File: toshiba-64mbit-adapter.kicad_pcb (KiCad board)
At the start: 2 copper layers, 18 x 55 mm, 9 parts, among them U1 TC5364205, U2 W29GL064C, U3 74HCT244, U4 74HCT244, U5 74HCT244, U6 74HCT244, U7 74HCT244, U8 TPS73633DBV

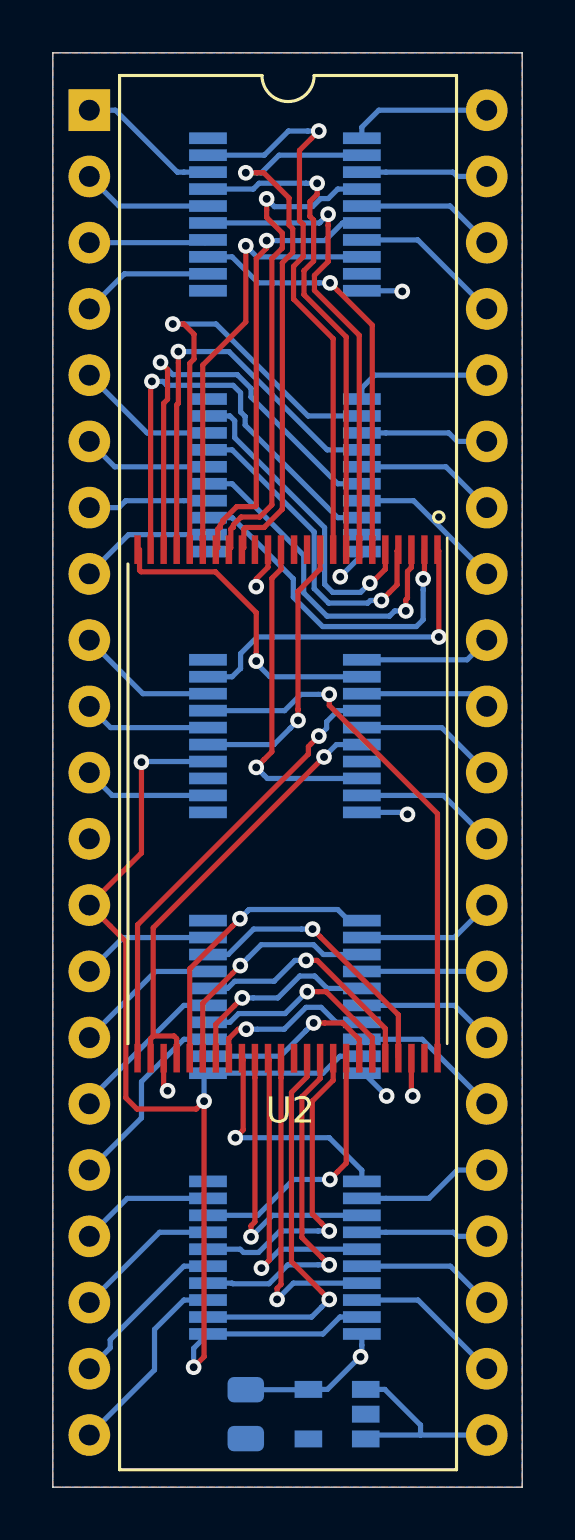
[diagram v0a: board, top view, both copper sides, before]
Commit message: Add 3 jumpers to allow picking between byte/word access
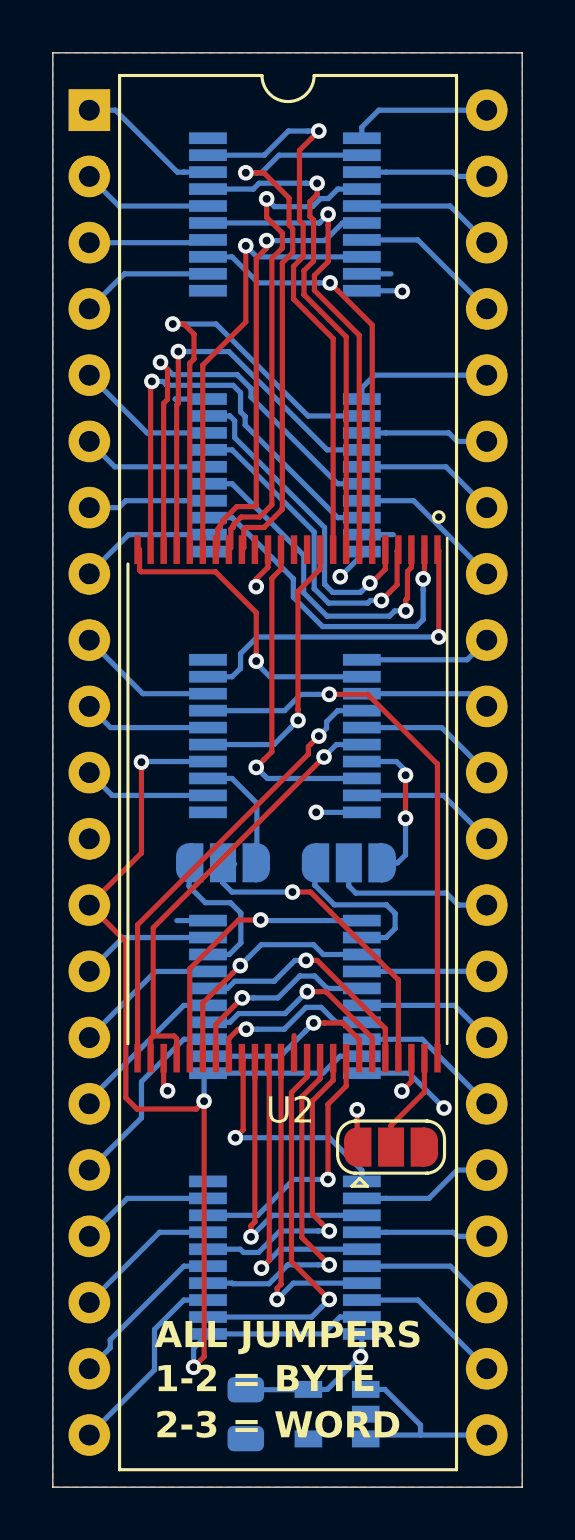
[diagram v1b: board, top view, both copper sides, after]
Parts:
- added JP1: SolderJumper_3_Open, Jumper:SolderJumper-3_P1.3mm_Open_RoundedPad1.0x1.5mm, B.Cu at (116.1, 89.9)
- added JP2: SolderJumper_3_Open, Jumper:SolderJumper-3_P1.3mm_Open_RoundedPad1.0x1.5mm, B.Cu at (121.0, 89.9)
- added JP3: SolderJumper_3_Open, Jumper:SolderJumper-3_P1.3mm_Open_RoundedPad1.0x1.5mm, F.Cu at (122.6, 100.8)
- U3, U4, U5, U6, U7: value 74HCT244 -> 74LVC244
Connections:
- U1 pad 30: /D15 -> /DA15
- U2 pad 15: Net-(U2-Pad15) -> unconnected-(U2-/BY-Pad15)
- U2 pad 45: /md15 -> /mad15
- U2 pad 47: +3V3 -> /BYTE
- U5 pad 17: GND -> /A-1
- U5 pad 3: Net-(U5-Pad3) -> /ma-1
- U8 pad 4: Net-(U8-Pad4) -> unconnected-(U8-NR-Pad4)
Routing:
- net /mad15: track 0.00 -> 12.2 mm, vias 0 -> 1
- net /DA15: track 0.00 -> 6.95 mm
- net GND: track 9.87 -> 16.0 mm, vias 3 -> 4
- net /A-1: track 0.00 -> 6.05 mm, vias 0 -> 2
- net /md15: track 10.7 -> 5.90 mm, vias 1 -> 0
- net /ma-1: track 0.00 -> 4.55 mm
- net /BYTE: track 0.00 -> 3.94 mm
- net +3V3: track 11.9 -> 15.1 mm
- net /D15: track 5.31 -> 6.38 mm
- net /ma16: track 20.6 -> 21.4 mm
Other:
- net class Default removed
- board text added: "1-2 = BYTE"
- board text added: "2-3 = WORD"
- board text added: "ALL JUMPERS"
- board text added: "CC0 v1.1 2019 ack v1"
- board text removed: "CC0 v1.1 2019"

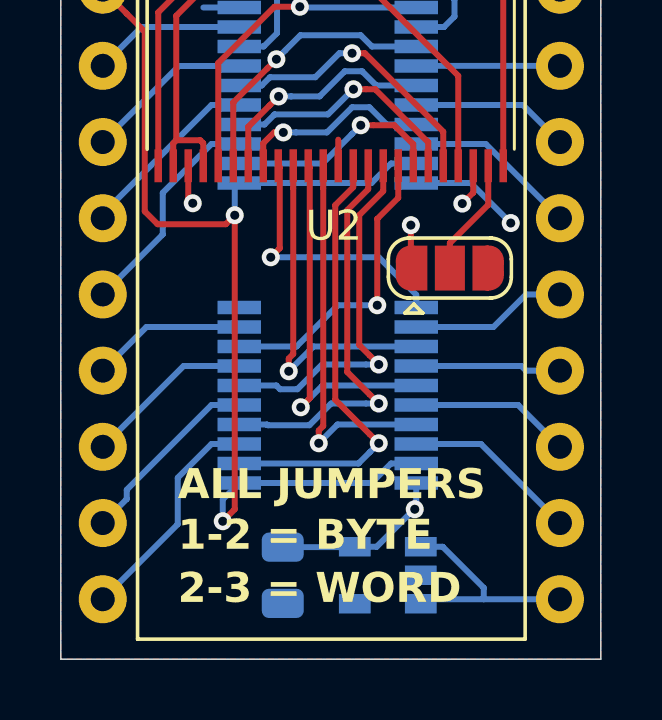
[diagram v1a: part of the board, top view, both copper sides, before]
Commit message: Switch the 2x data line LVC244s to HCT244s
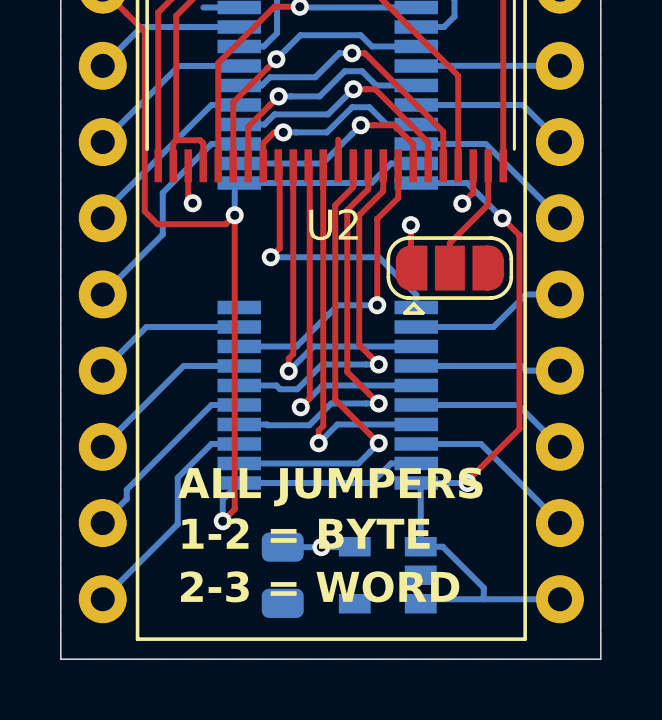
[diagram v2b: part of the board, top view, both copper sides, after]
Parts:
- U6, U7: value 74LVC244 -> 74HCT244
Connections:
- U6 pad 20: +3V3 -> +5V
- U7 pad 20: +3V3 -> +5V
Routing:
- net +5V: track 7.75 -> 24.6 mm, vias 0 -> 2
- net +3V3: track 15.1 -> 7.89 mm, vias 5 -> 4
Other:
- board text added: "CC0 v1.1 2019 ack v2"
- board text added: "HCT244"
- board text added: "LVC244"
- board text removed: "CC0 v1.1 2019 ack v1"
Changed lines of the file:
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@@
 		)
 		(sheetname "Root")
-		(sheetfile "/Users/jwestfall/Downloads/toshiba-64mbit-adapter-master/toshiba-64mbit-adapter.sch")
+		(sheetfile "toshiba-64mbit-adapter.kicad_sch")
 		(attr smd)
 		(fp_line
@@
 		)
 		(sheetname "Root")
-		(sheetfile "/Users/jwestfall/Downloads/toshiba-64mbit-adapter-master/toshiba-64mbit-adapter.sch")
+		(sheetfile "toshiba-64mbit-adapter.kicad_sch")
 		(attr through_hole)
 		(fp_line
@@
 		(property ki_fp_filters "SolderJumper*Open*")
 		(sheetname "Root")
-		(sheetfile "/Users/jwestfall/Downloads/toshiba-64mbit-adapter-master/toshiba-64mbit-adapter.sch")
+		(sheetfile "toshiba-64mbit-adapter.kicad_sch")
 		(zone_connect 1)
 		(attr exclude_from_pos_files exclude_from_bom)
@@
 		(property ki_fp_filters "TSSOP*4.4x6.5mm*P0.65mm* SSOP*4.4x6.5mm*P0.65mm*")
 		(sheetname "Root")
-		(sheetfile "/Users/jwestfall/Downloads/toshiba-64mbit-adapter-master/toshiba-64mbit-adapter.sch")
+		(sheetfile "toshiba-64mbit-adapter.kicad_sch")
 		(attr smd)
 		(fp_line
@@
 		(property ki_fp_filters "TSSOP*4.4x6.5mm*P0.65mm* SSOP*4.4x6.5mm*P0.65mm*")
 		(sheetname "Root")
-		(sheetfile "/Users/jwestfall/Downloads/toshiba-64mbit-adapter-master/toshiba-64mbit-adapter.sch")
+		(sheetfile "toshiba-64mbit-adapter.kicad_sch")
 		(attr smd)
 		(fp_line
@@
 			)
 		)
-		(property "Value" "74LVC244"
+		(property "Value" "74HCT244"
 			(at 0 -4.3 0)
 			(layer "B.Fab")
@@
 		(property ki_fp_filters "TSSOP*4.4x6.5mm*P0.65mm* SSOP*4.4x6.5mm*P0.65mm*")
 		(sheetname "Root")
-		(sheetfile "/Users/jwestfall/Downloads/toshiba-64mbit-adapter-master/toshiba-64mbit-adapter.sch")
+		(sheetfile "toshiba-64mbit-adapter.kicad_sch")
 		(attr smd)
 		(fp_line
@@
 			(size 1.45 0.45)
 			(layers "B.Cu" "B.Paste" "B.Mask")
-			(net 43 "+3V3")
+			(net 40 "+5V")
 			(pinfunction "VCC")
 			(pintype "power_in")
@@
 			)
 		)
-		(property "Value" "74LVC244"
+		(property "Value" "74HCT244"
 			(at 0 -4.3 0)
 			(layer "B.Fab")
@@
 		(property ki_fp_filters "TSSOP*4.4x6.5mm*P0.65mm* SSOP*4.4x6.5mm*P0.65mm*")
 		(sheetname "Root")
-		(sheetfile "/Users/jwestfall/Downloads/toshiba-64mbit-adapter-master/toshiba-64mbit-adapter.sch")
+		(sheetfile "toshiba-64mbit-adapter.kicad_sch")
 		(attr smd)
 		(fp_line
@@
 			(size 1.45 0.45)
 			(layers "B.Cu" "B.Paste" "B.Mask")
-			(net 43 "+3V3")
+			(net 40 "+5V")
 			(pinfunction "VCC")
 			(pintype "power_in")
@@
 		(property "Reference" "U8"
 			(at -2.7 0 -90)
+			(unlocked yes)
 			(layer "B.SilkS")
 			(effects
@@
 		(property ki_fp_filters "SOT?23*")
 		(sheetname "Root")
-		(sheetfile "/Users/jwestfall/Downloads/toshiba-64mbit-adapter-master/toshiba-64mbit-adapter.sch")
+		(sheetfile "toshiba-64mbit-adapter.kicad_sch")
 		(attr smd)
 		(fp_line
@@
 		(property ki_fp_filters "TSSOP*4.4x6.5mm*P0.65mm* SSOP*4.4x6.5mm*P0.65mm*")
 		(sheetname "Root")
-		(sheetfile "/Users/jwestfall/Downloads/toshiba-64mbit-adapter-master/toshiba-64mbit-adapter.sch")
+		(sheetfile "toshiba-64mbit-adapter.kicad_sch")
 		(attr smd)
 		(fp_line
@@
 		(tags "capacitor")
 		(property "Reference" "C1"
-			(at 0 -1.7 90)
+			(at 0 -1.7 -90)
+			(unlocked yes)
 			(layer "B.SilkS")
 			(effects
@@
 		(property ki_fp_filters "C_*")
 		(sheetname "Root")
-		(sheetfile "/Users/jwestfall/Downloads/toshiba-64mbit-adapter-master/toshiba-64mbit-adapter.sch")
+		(sheetfile "toshiba-64mbit-adapter.kicad_sch")
 		(attr smd)
 		(fp_line
@@
 		(property ki_fp_filters "SolderJumper*Open*")
 		(sheetname "Root")
-		(sheetfile "/Users/jwestfall/Downloads/toshiba-64mbit-adapter-master/toshiba-64mbit-adapter.sch")
+		(sheetfile "toshiba-64mbit-adapter.kicad_sch")
 		(zone_connect 1)
 		(attr exclude_from_pos_files exclude_from_bom)
@@
 		(property ki_fp_filters "SolderJumper*Open*")
 		(sheetname "Root")
-		(sheetfile "/Users/jwestfall/Downloads/toshiba-64mbit-adapter-master/toshiba-64mbit-adapter.sch")
+		(sheetfile "toshiba-64mbit-adapter.kicad_sch")
 		(zone_connect 1)
 		(attr exclude_from_pos_files exclude_from_bom)
@@
 		)
 	)
-	(gr_text "CC0 v1.1 2019 ack v1"
+	(gr_text "HCT244"
+		(at 117.9 108 270)
+		(layer "B.SilkS")
+		(effects
+			(font
+				(size 1 1)
+				(thickness 0.15)
+			)
+			(justify left bottom mirror)
+		)
+	)
+	(gr_text "CC0 v1.1 2019 ack v2"
 		(at 113.09 89.97 270)
 		(layer "B.SilkS")
@@
 		)
 	)
+	(gr_text "LVC244"
+		(at 117.9 77.9 270)
+		(layer "B.SilkS")
+		(effects
+			(font
+				(size 1 1)
+				(thickness 0.15)
+			)
+			(justify left bottom mirror)
+		)
+	)
+	(gr_text "LVC244"
+		(at 117.9 87.9 270)
+		(layer "B.SilkS")
+		(effects
+			(font
+				(size 1 1)
+				(thickness 0.15)
+			)
+			(justify left bottom mirror)
+		)
+	)
+	(gr_text "HCT244"
+		(at 117.9 98 270)
+		(layer "B.SilkS")
+		(effects
+			(font
+				(size 1 1)
+				(thickness 0.15)
+			)
+			(justify left bottom mirror)
+		)
+	)
+	(gr_text "LVC244"
+		(at 117.9 67.9 270)
+		(layer "B.SilkS")
+		(effects
+			(font
+				(size 1 1)
+				(thickness 0.15)
+			)
+			(justify left bottom mirror)
+		)
+	)
 	(gr_text "2-3 = WORD"
 		(at 113.5 112.01 0)
@@
 	)
 	(segment
+		(start 124.32103 99.09897)
+		(end 124.89 99.66794)
+		(width 0.2)
+		(layer "F.Cu")
+		(net 40)
+	)
+	(segment
+		(start 124.89 106.12)
+		(end 123.12 107.89)
+		(width 0.2)
+		(layer "F.Cu")
+		(net 40)
+	)
+	(segment
+		(start 124.89 99.66794)
+		(end 124.89 106.12)
+		(width 0.2)
+		(layer "F.Cu")
+		(net 40)
+	)
+	(via
+		(at 123.16 107.925)
+		(size 0.6)
+		(drill 0.3)
+		(layers "F.Cu" "B.Cu")
+		(net 40)
+	)
+	(via
+		(at 124.32103 99.09897)
+		(size 0.6)
+		(drill 0.3)
+		(layers "F.Cu" "B.Cu")
+		(net 40)
+	)
+	(segment
+		(start 124.32103 99.09897)
+		(end 124.321029 99.09897)
+		(width 0.2)
+		(layer "B.Cu")
+		(net 40)
+	)
+	(segment
+		(start 121.6 110.05)
+		(end 121.6 108.075)
+		(width 0.2)
+		(layer "B.Cu")
+		(net 40)
+	)
+	(segment
+		(start 121.45 107.925)
+		(end 123.16 107.925)
+		(width 0.2)
+		(layer "B.Cu")
+		(net 40)
+	)
+	(segment
+		(start 123.147059 97.925)
+		(end 121.45 97.925)
+		(width 0.2)
+		(layer "B.Cu")
+		(net 40)
+	)
+	(segment
+		(start 123.16 107.925)
+		(end 123.165 107.925)
+		(width 0.2)
+		(layer "B.Cu")
+		(net 40)
+	)
+	(segment
 		(start 126.24 111.8)
 		(end 123.7 111.8)
@@
 	)
 	(segment
+		(start 124.321029 99.09897)
+		(end 123.147059 97.925)
+		(width 0.2)
+		(layer "B.Cu")
+		(net 40)
+	)
+	(segment
 		(start 123.7 111.8)
 		(end 123.7 111.42)
@@
 	)
 	(via
-		(at 124.6 99.26)
+		(at 118.29 110.0625)
 		(size 0.6)
 		(drill 0.3)
@@
 	)
 	(via
-		(at 121.4 108.8)
-		(size 0.6)
-		(drill 0.3)
-		(layers "F.Cu" "B.Cu")
-		(net 43)
-	)
-	(via
 		(at 120.621612 78.889196)
 		(size 0.6)
@@
 	)
 	(segment
-		(start 123.265 97.925)
-		(end 121.45 97.925)
-		(width 0.2)
-		(layer "B.Cu")
-		(net 43)
-	)
-	(segment
 		(start 122.975 67.925)
 		(end 123 67.95)
@@
 	)
 	(segment
-		(start 121.45 108.73)
-		(end 121.45 108.75)
-		(width 0.2)
-		(layer "B.Cu")
-		(net 43)
-	)
-	(segment
 		(start 119.3875 110.0625)
 		(end 119.4 110.05)
@@
 	)
 	(segment
-		(start 121.45 108.75)
-		(end 121.4 108.8)
-		(width 0.2)
-		(layer "B.Cu")
-		(net 43)
-	)
-	(segment
-		(start 121.45 108.35)
-		(end 121.45 107.925)
-		(width 0.2)
-		(layer "B.Cu")
-		(net 43)
-	)
-	(segment
-		(start 120.13 110.05)
-		(end 121.45 108.73)
-		(width 0.2)
-		(layer "B.Cu")
-		(net 43)
-	)
-	(segment
-		(start 119.4 110.05)
-		(end 120.13 110.05)
-		(width 0.2)
-		(layer "B.Cu")
-		(net 43)
-	)
-	(segment
-		(start 121.45 108.73)
-		(end 121.45 108.35)
-		(width 0.2)
-		(layer "B.Cu")
-		(net 43)
-	)
-	(segment
-		(start 124.6 99.26)
-		(end 123.265 97.925)
+		(start 118.29 110.0625)
+		(end 119.3875 110.0625)
 		(width 0.2)
 		(layer "B.Cu")
@@
 	(segment
 		(start 117 110.0625)
-		(end 119.3875 110.0625)
+		(end 118.29 110.0625)
 		(width 0.2)
 		(layer "B.Cu")
